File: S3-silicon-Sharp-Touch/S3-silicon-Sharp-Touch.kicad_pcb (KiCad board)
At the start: 4 copper layers, 77.8 x 44.7 mm, 65 parts, among them IC1 ESP32-S3FN8, J1 USB_C_Receptacle_USB2.0, J2 Conn_01x06_Socket, J3 Conn_01x11_Socket, J4 SM04B-SRSS-TB_LF__SN_, J5 FH52-10S-0.5SH_99, J6 5024260810, J7 S2B-PH-SM4-TB_LF__SN_, Q1 MMBT3904, Q2 MMBT3904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

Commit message: S3 PCB 3D stl file
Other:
- board text removed: "IO0"
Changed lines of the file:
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@@
-    (effects (font (size 0.9 0.9) (thickness 0.15)) (justify left bottom))
-  )
-  (gr_text "IO0" (at 38.827143 50.05) (layer "F.SilkS")
     (effects (font (size 0.9 0.9) (thickness 0.15)) (justify left bottom))
   )

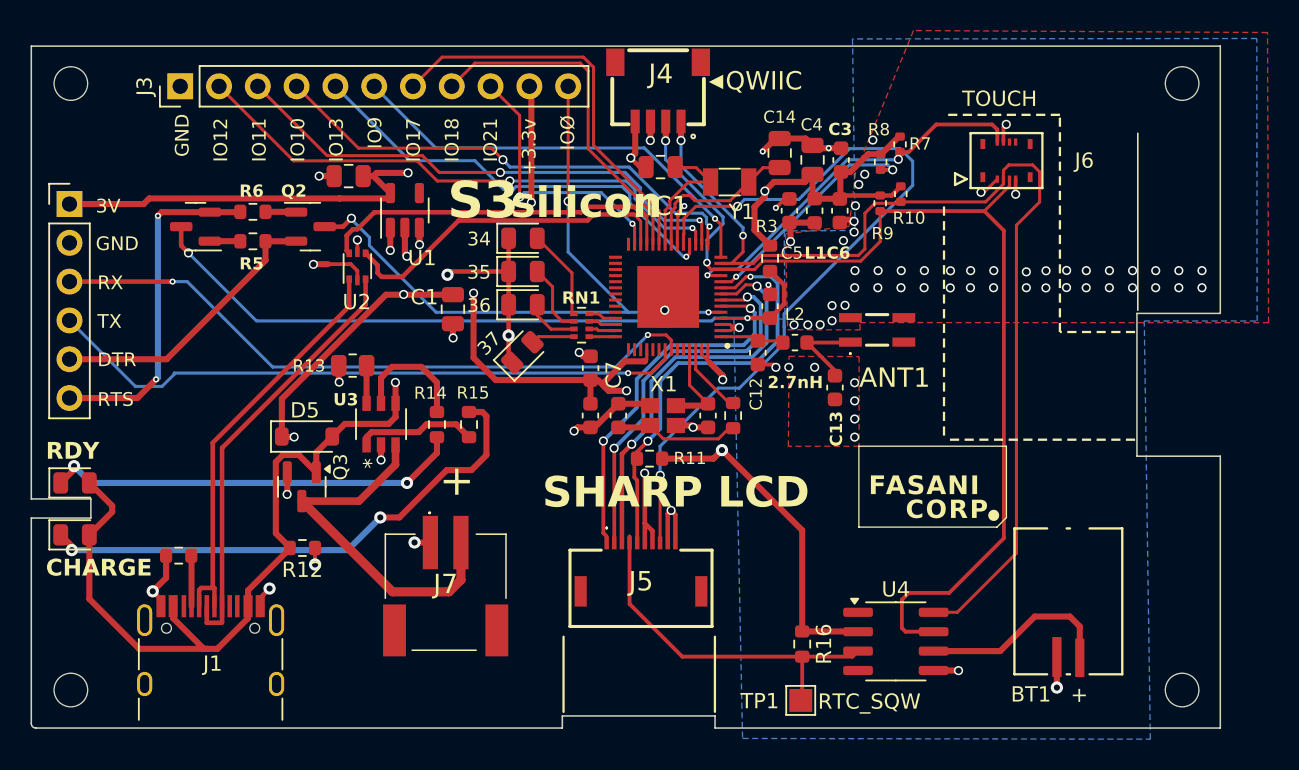
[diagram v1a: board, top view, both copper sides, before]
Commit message: Update RTC with RV-3032
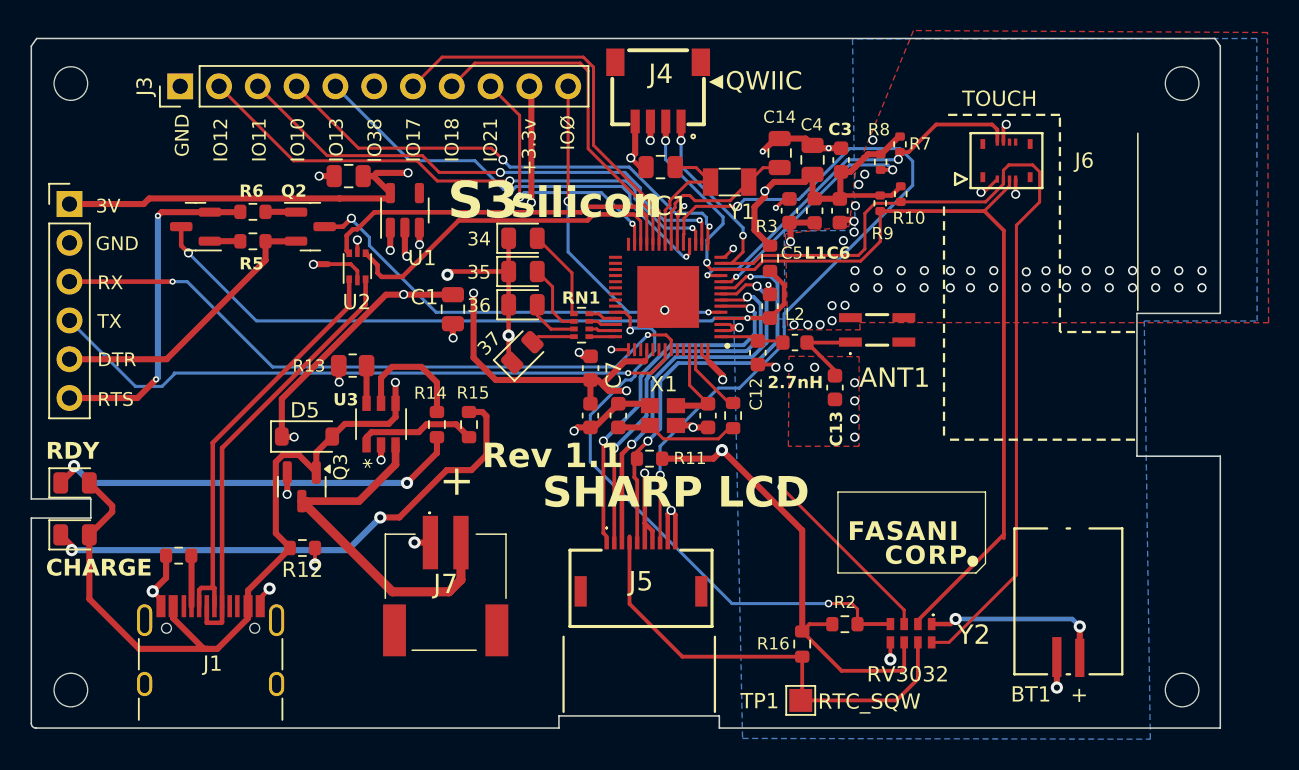
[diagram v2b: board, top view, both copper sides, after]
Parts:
- removed U4: DS3231MZ, Package_SO:SOIC-8_3.9x4.9mm_P1.27mm
- added R2: 10 K, Resistor_SMD:R_0603_1608Metric, F.Cu at (80.9, 69.3)
- added Y2: RV-3032-C7, foot_sharp:RV3032C7, F.Cu at (85.2, 69.9)
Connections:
- IC1 pad 14: /IO9 -> /RTC_INT
- IC1 pad 38: unconnected-(IC1-GPIO33-Pad38) -> /RTC_EVI
- IC1 pad 43: unconnected-(IC1-GPIO38-Pad43) -> /IO38
- J3 pad 6: /IO9 -> /IO38
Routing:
- net /RTC_EVI: track 0.00 -> 38.9 mm, vias 0 -> 2
- net /RTC_INT: track 0.00 -> 31.1 mm, vias 0 -> 2
- net /IO9: track 28.6 -> 0.00 mm, vias 1 -> 0
- net /IO38: track 0.00 -> 24.8 mm, vias 0 -> 1
- net VDD33: track 178.3 -> 186.3 mm
- net /RTC_SQW: track 23.1 -> 30.0 mm
- net /SDA: track 69.5 -> 65.4 mm
- net /SCL: track 69.4 -> 71.2 mm
- net VDD_RTC: track 12.8 -> 12.1 mm, vias 0 -> 2
- net GND: track 60.3 -> 59.8 mm
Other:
- board size 77.8 x 44.7 mm -> 77.8 x 45.2 mm
- board text added: "IO38"
- board text added: "RV3032"
- board text added: "Rev 1.1"
- board text removed: "IO9"

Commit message: 1.1 cut-outs
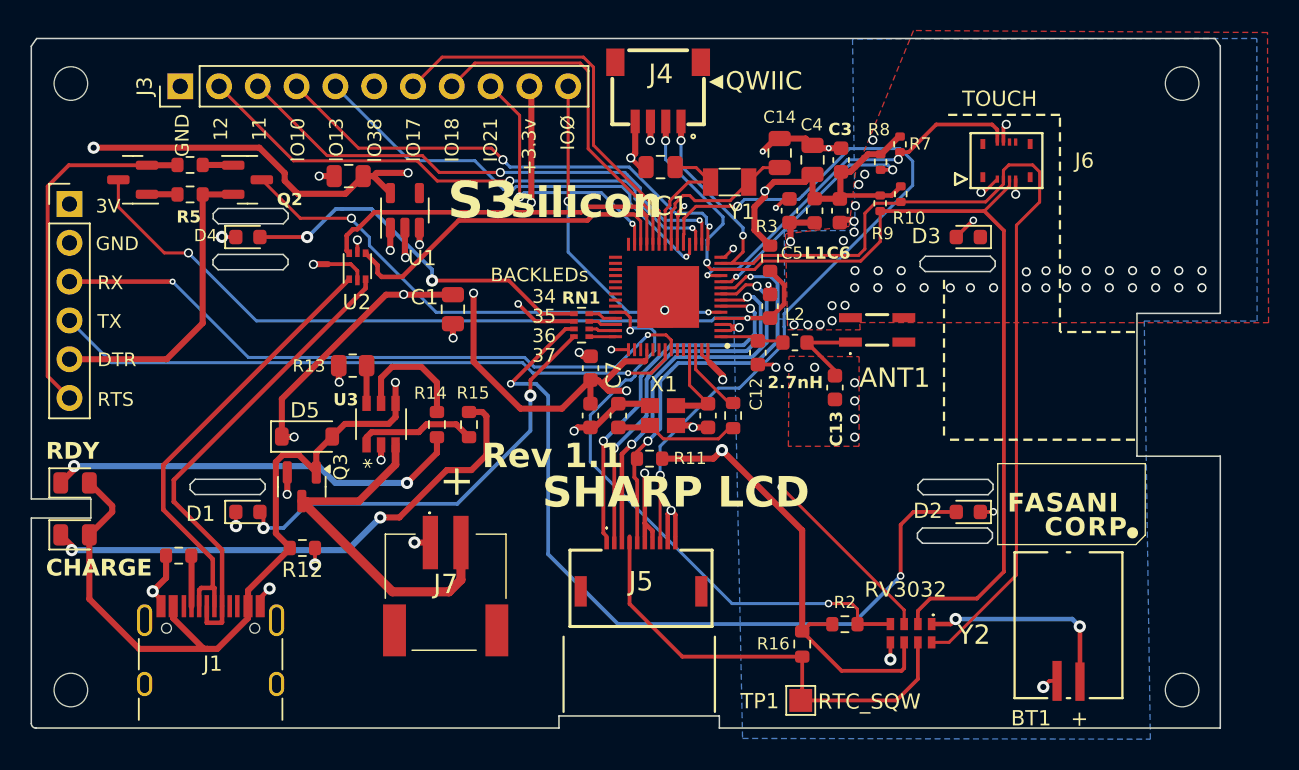
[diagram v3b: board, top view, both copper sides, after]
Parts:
- D1: value LED GREEN -> WHITE LEDs; footprint LED_SMD:LED_0805_2012Metric -> LED_SMD:LED_0603_1608Metric
- D2, D3, D4: footprint LED_SMD:LED_0805_2012Metric -> LED_SMD:LED_0603_1608Metric
- moved D2 32.2 mm to (89.0, 62.0), turned to 180 degrees
- moved D3 29.2 mm to (89.0, 44.0), turned to 180 degrees
- moved D1 20.8 mm to (41.8, 62.0), turned to 0 degrees
- moved D4 18.0 mm to (41.8, 44.0)
- moved Q1 5.13 mm to (34.3, 40.2)
- moved Q2 5.13 mm to (41.8, 40.2)
- moved R5 5.13 mm to (38.0, 41.2)
- moved R6 5.13 mm to (38.0, 39.3)
- moved BT1 1.56 mm to (95.6, 69.4)
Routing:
- net Net-(D2-A): track 3.18 -> 52.4 mm, vias 0 -> 2
- net Net-(D3-A): track 4.42 -> 51.4 mm, vias 0 -> 2
- net Net-(D1-A): track 2.44 -> 28.6 mm, vias 0 -> 2
- net Net-(D4-A): track 5.88 -> 24.6 mm, vias 0 -> 2
- net GND: track 59.8 -> 49.4 mm, vias 77 -> 74
- net /CHIP_PU: track 47.8 -> 53.5 mm
- net VDD33: track 186.3 -> 191.5 mm, vias 10 -> 11
- net /IO0: track 45.9 -> 50.9 mm
- net /USB_U_D-: track 27.2 -> 29.9 mm
- net /USB_U_D+: track 28.5 -> 31.1 mm
- net VDD_RTC: track 12.1 -> 13.7 mm
- net /SDA: track 65.4 -> 66.9 mm
- net /DTR: track 18.8 -> 20.1 mm
- net /RTS: track 22.4 -> 23.5 mm, vias 2 -> 0
- net TX: track 42.2 -> 41.4 mm
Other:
- outline, holes or cut-outs redrawn
- board text added: "11"
- board text added: "12"
- board text added: "BACKLEDs"
- board text removed: "IO11"
- board text removed: "IO12"
